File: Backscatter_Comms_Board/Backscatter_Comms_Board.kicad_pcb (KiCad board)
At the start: 2 copper layers, 43 parts, among them J1 Conn_01x03, J2 Conn_01x07, J3 Conn_01x02, M1 MNMOS, M2 MNMOS, T1 SP-48, U1 ADG919BRMZ, U2 ADG841YKSZ-REEL7, U3 NCS2200SQ2T2G

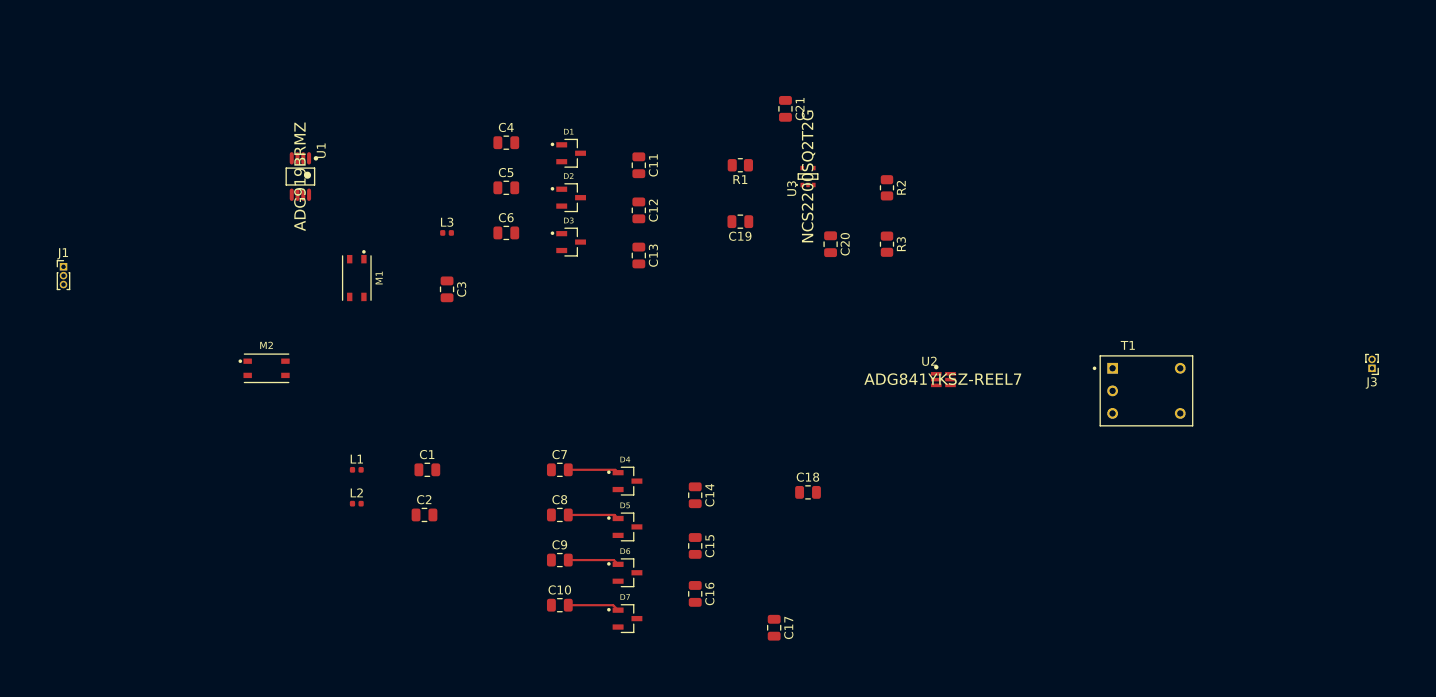
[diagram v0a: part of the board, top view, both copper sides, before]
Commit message: rolled back cause the PCB broke
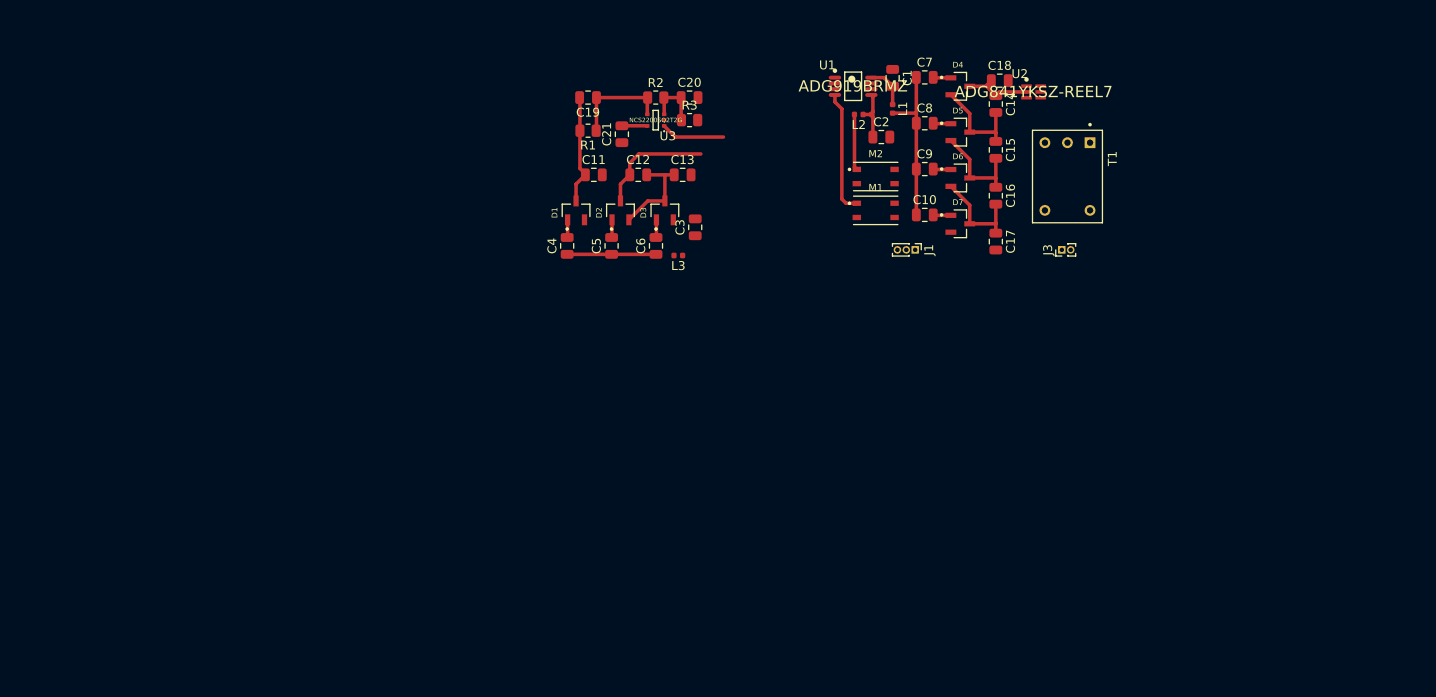
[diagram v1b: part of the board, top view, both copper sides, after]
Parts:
- moved J1 95.9 mm to (137.8, 89.5), turned to 270 degrees
- moved L1 72.7 mm to (135.3, 73.7), turned to 270 degrees
- moved M2 71.9 mm to (133.3, 81.3)
- moved L2 71.5 mm to (131.4, 74.3), turned to 180 degrees
- moved C1 68.5 mm to (135.3, 70.2), turned to 270 degrees
- moved C2 66.8 mm to (134.0, 76.8)
- moved U1 63.1 mm to (130.8, 71.1), turned to 0 degrees
- moved C7 60.3 mm to (138.9, 70.1)
- moved C8 60.3 mm to (138.9, 75.3)
- moved C9 60.2 mm to (138.9, 80.4)
- moved C10 60.2 mm to (138.9, 85.6)
- moved M1 58.9 mm to (133.3, 85.1), turned to 0 degrees
- moved D7 58.1 mm to (142.9, 86.6)
- moved D5 58.1 mm to (142.9, 76.3)
- moved D6 58.1 mm to (142.9, 81.4)
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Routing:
- net Net-(C10-Pad1): track 0.00 -> 18.2 mm
- net Ant: track 0.00 -> 13.9 mm
- net Vrect: track 0.00 -> 13.1 mm
- net Net-(C11-Pad1): track 0.00 -> 12.3 mm
- net Net-(C19-Pad1): track 0.00 -> 11.4 mm
- net Net-(C14-Pad2): track 0.00 -> 11.3 mm
- net Net-(C16-Pad2): track 0.00 -> 11.3 mm
- net Net-(C15-Pad2): track 0.00 -> 11.3 mm
- net Net-(C12-Pad2): track 0.00 -> 11.0 mm
- net Net-(C4-Pad1): track 0.00 -> 10.0 mm
- net Stage4: track 0.00 -> 7.86 mm
- net RF_RX: track 0.00 -> 7.19 mm
- net Net-(C2-Pad1): track 0.00 -> 6.50 mm
- net Net-(C20-Pad1): track 0.00 -> 6.41 mm
- net Net-(J1-Pad3): track 0.00 -> 6.29 mm
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
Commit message: Too big version
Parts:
- added AE1: Antenna_Chip, Connector_Coaxial:U.FL_Molex_MCRF_73412-0110_Vertical, F.Cu at (88.9, 38.1)
- added C22: 0.01uF, Capacitor_SMD:C_0805_2012Metric, F.Cu at (80.6, 35.2)
- J1: value Conn_01x03 -> SPK_IN; footprint Connector_PinHeader_1.00mm:PinHeader_1x03_P1.00mm_Vertical -> Local Components:Multi-purpose_mic
- J2: value Conn_01x07 -> Conn_01x09; footprint Connector_PinHeader_1.00mm:PinHeader_1x07_P1.00mm_Vertical -> Connector_PinHeader_1.00mm:PinHeader_1x09_P1.00mm_Vertical
- M2: value MNMOS -> DNP
- moved T1 88.5 mm to (83.8, 28.6)
- moved J3 87.0 mm to (83.2, 39.4)
- moved J2 81.1 mm to (104.8, 40.6), turned to 90 degrees
- moved M1 69.2 mm to (90.8, 30.5), turned to 90 degrees
- moved J1 67.2 mm to (94.6, 38.1), turned to 0 degrees
- moved C17 64.3 mm to (110.5, 35.6), turned to 0 degrees
- moved C10 62.8 mm to (99.5, 36.7)
- moved C14 62.8 mm to (107.5, 24.2)
- moved C16 62.8 mm to (107.5, 34.5)
- moved C2 62.8 mm to (94.6, 27.9)
- moved C7 62.8 mm to (99.5, 21.2)
- moved C8 62.8 mm to (99.5, 26.4)
- moved C9 62.8 mm to (99.5, 31.5)
- moved D4 62.8 mm to (103.5, 22.2)
- moved D5 62.8 mm to (103.5, 27.4)
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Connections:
- C21 pad 2: Net-(C21-Pad2) -> RX_EN
- J2 pad 1: Stage4 -> Vstore
- J2 pad 2: Vrect -> RX_EN
- J2 pad 3: RF_RX -> Stage4
- J2 pad 4: UPLINK_SR -> Vrect
- J2 pad 5: SPK_EN -> RF_RX
- J2 pad 6: AN_EN -> RF_TX
- J2 pad 7: Ant -> UPLINK_SR
- U3 pad 5: Net-(C21-Pad2) -> RX_EN
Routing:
- net Ant: track 13.9 -> 1.89 mm
- net Net-(J1-Pad3): track 6.29 -> 0.00 mm
- net Net-(C16-Pad2): track 11.3 -> 5.09 mm
- net Vrect: track 13.1 -> 9.76 mm
- net Net-(C11-Pad1): track 12.3 -> 8.97 mm
- net Net-(C12-Pad2): track 11.0 -> 8.03 mm
- net RX_EN: track 0.00 -> 2.87 mm
- net Net-(C21-Pad2): track 2.87 -> 0.00 mm
- net Net-(C10-Pad1): track 18.2 -> 15.5 mm
- net Net-(C14-Pad2): track 11.3 -> 13.3 mm
- net Net-(C15-Pad2): track 11.3 -> 12.1 mm
- added copper zone on B.Cu, net (none)
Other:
- board outline added: 51.4 x 23.5 mm
- board text added: "CHANGE ANT TO UFL CONNECTOR"

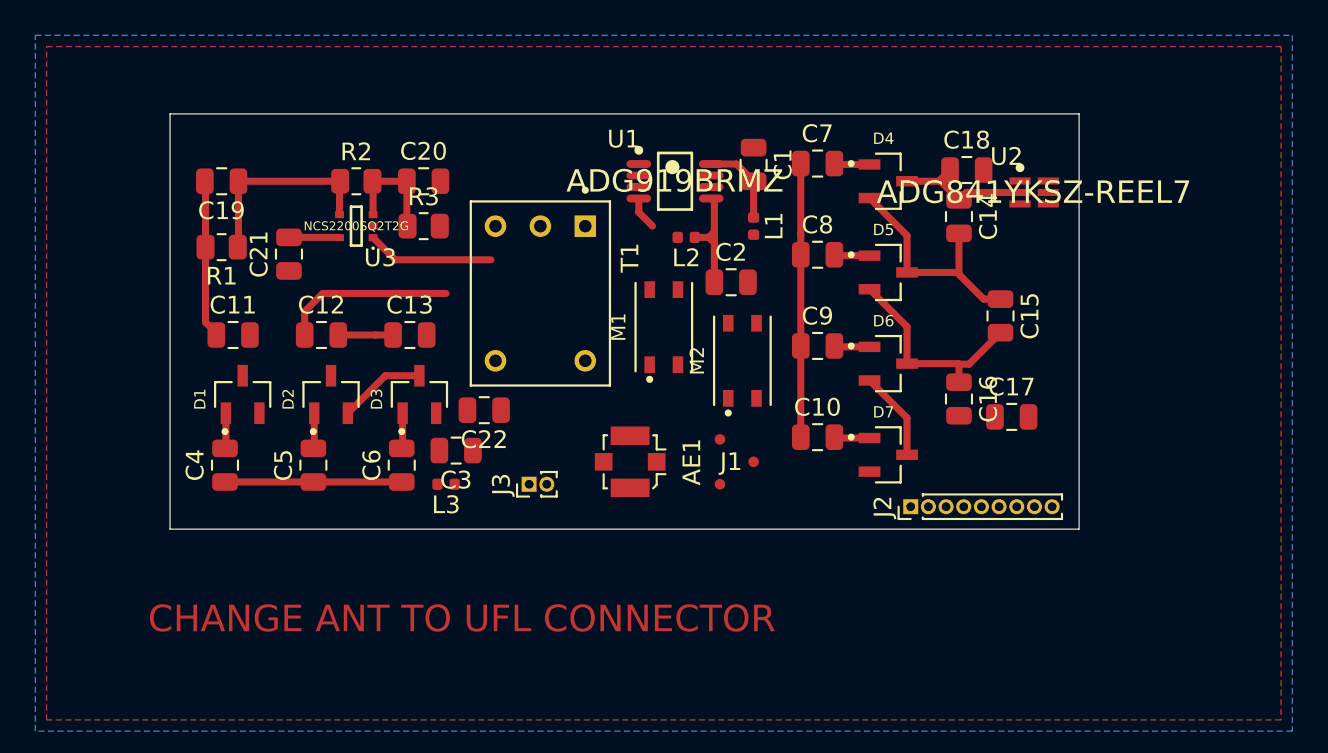
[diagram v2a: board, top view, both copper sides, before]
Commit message: V2 incorporating first round review
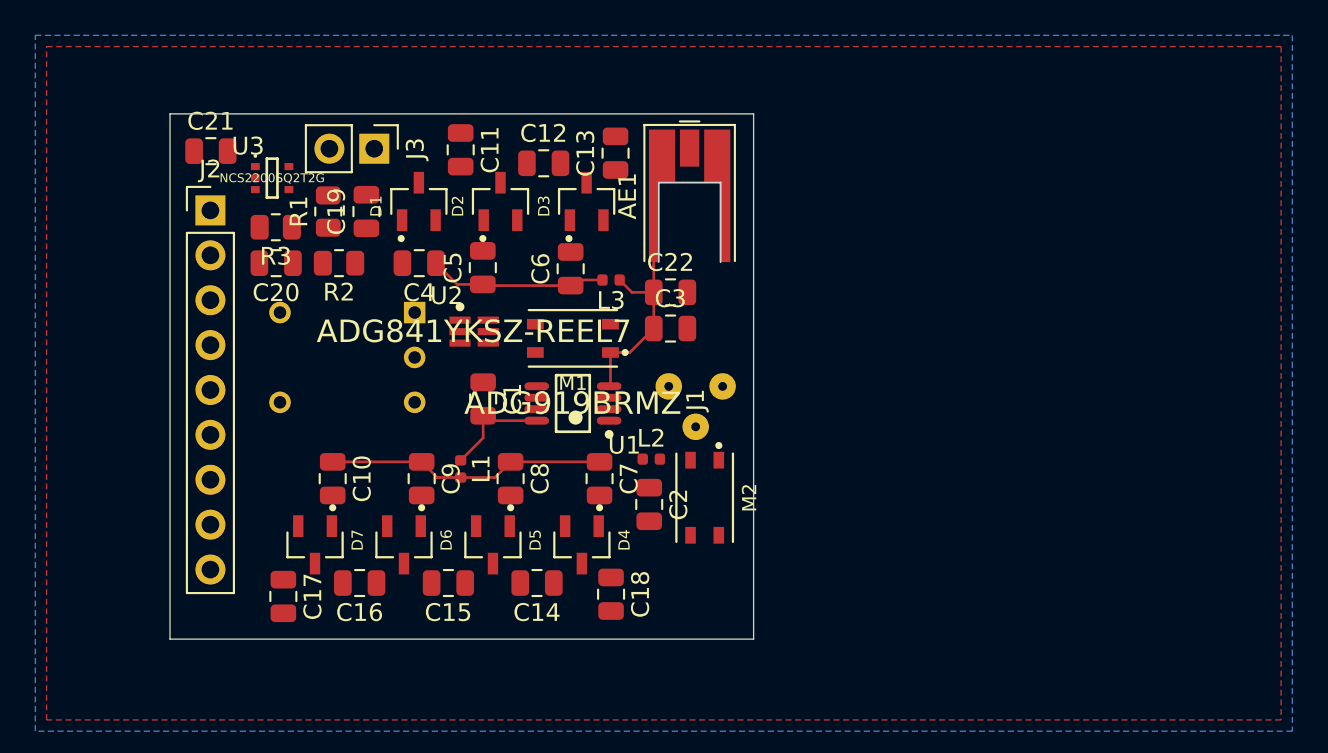
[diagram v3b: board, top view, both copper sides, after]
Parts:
- AE1: footprint Connector_Coaxial:U.FL_Molex_MCRF_73412-0110_Vertical -> Connector_Coaxial:MMCX_Molex_73415-0961_Horizontal_1.0mm-PCB
- J2: footprint Connector_PinHeader_1.00mm:PinHeader_1x09_P1.00mm_Vertical -> Connector_PinHeader_2.54mm:PinHeader_1x09_P2.54mm_Vertical
- J3: footprint Connector_PinHeader_1.00mm:PinHeader_1x02_P1.00mm_Vertical -> Connector_PinHeader_2.54mm:PinHeader_1x02_P2.54mm_Vertical
- T1: moved to B.Cu
- moved J2 43.0 mm to (65.2, 23.9), turned to 0 degrees
- moved C17 42.4 mm to (69.3, 45.7), turned to 270 degrees
- moved C16 35.5 mm to (73.6, 45.0), turned to 180 degrees
- moved C15 34.7 mm to (78.6, 45.0), turned to 180 degrees
- moved D7 32.8 mm to (71.1, 42.8), turned to 270 degrees
- moved U2 32.7 mm to (80.1, 30.7)
- moved C14 31.6 mm to (83.6, 45.0), turned to 180 degrees
- moved C18 31.3 mm to (87.8, 45.6), turned to 270 degrees
- moved D6 29.3 mm to (76.1, 42.8), turned to 270 degrees
- moved C10 27.5 mm to (72.1, 39.1), turned to 270 degrees
- moved D5 27.2 mm to (81.1, 42.8), turned to 270 degrees
- moved D4 26.9 mm to (86.2, 42.8), turned to 270 degrees
- moved C9 23.6 mm to (77.1, 39.1), turned to 270 degrees
- moved C7 21.7 mm to (87.2, 39.1), turned to 270 degrees
- moved L1 21.5 mm to (79.3, 38.5)
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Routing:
- net Ant: track 1.89 -> 17.1 mm
- net Net-(C14-Pad2): track 13.3 -> 0.00 mm
- net Net-(C15-Pad2): track 12.1 -> 0.00 mm
- net Net-(C19-Pad1): track 11.4 -> 0.00 mm
- net Vrect: track 9.76 -> 0.00 mm
- net Net-(C11-Pad1): track 8.97 -> 0.00 mm
- net Net-(C12-Pad2): track 8.03 -> 0.00 mm
- net Stage4: track 7.86 -> 0.00 mm
- net RF_RX: track 7.19 -> 0.00 mm
- net Net-(C2-Pad1): track 6.50 -> 0.00 mm
- net Net-(C20-Pad1): track 6.41 -> 0.00 mm
- net Net-(C16-Pad2): track 5.09 -> 0.00 mm
- net RX_EN: track 2.87 -> 0.00 mm
- net Net-(C6-Pad2): track 2.01 -> 0.00 mm
- net Net-(C5-Pad2): track 2.01 -> 0.00 mm
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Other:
- board size 51.4 x 23.5 mm -> 33 x 29.7 mm
- net class Default: clearance 0.2 -> 0.1524; trace_width 0.25 -> 0.1524
- rule trace_clearance: 0.2 -> 0.1524
- rule trace_min: 0.2 -> 0.1524
- board text removed: "CHANGE ANT TO UFL CONNECTOR"

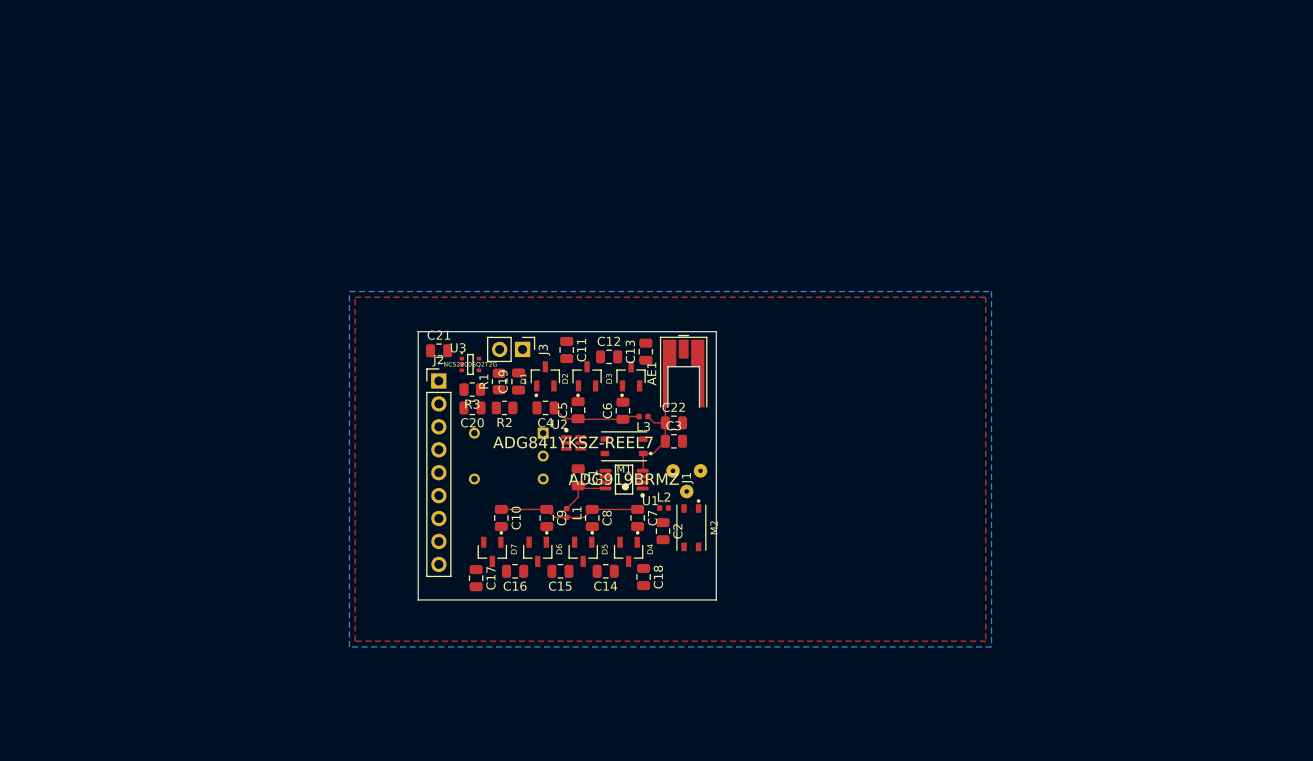
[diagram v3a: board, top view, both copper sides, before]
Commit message: Redid Board layou
Even smaller rf path and other fun things
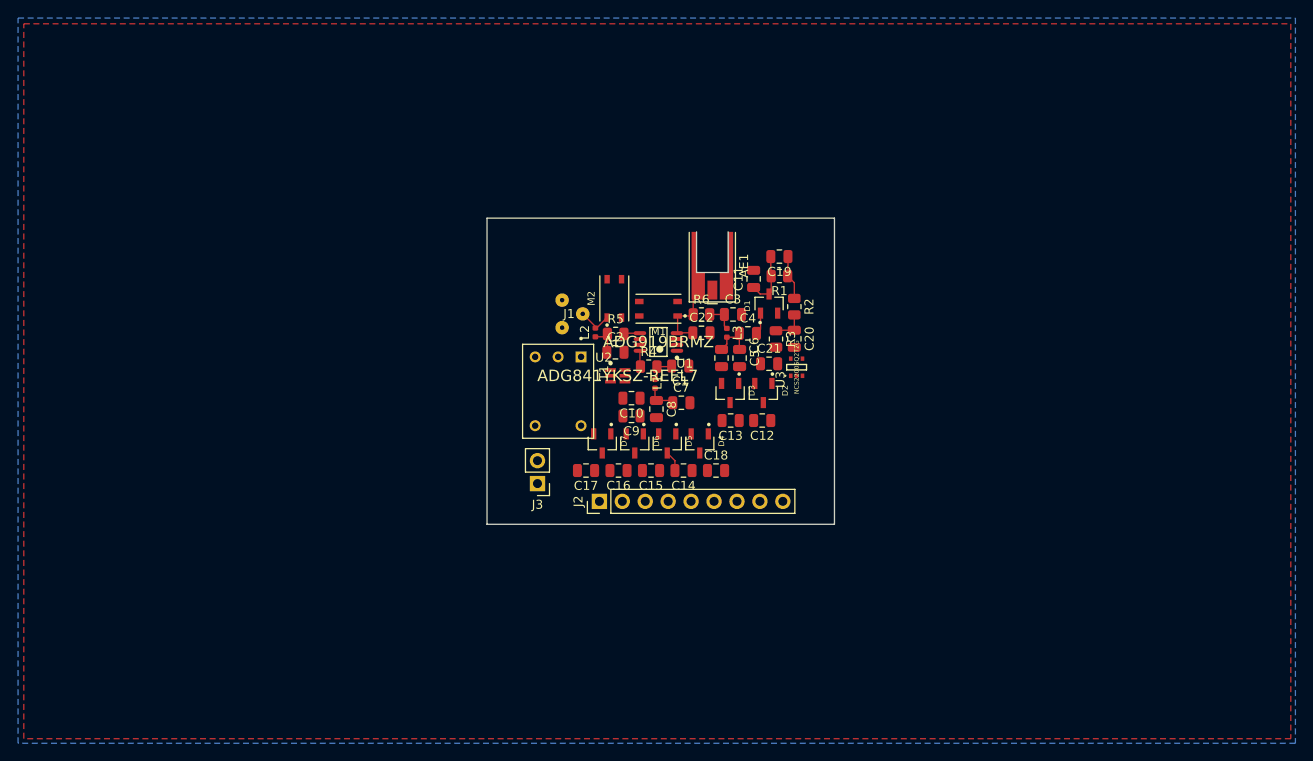
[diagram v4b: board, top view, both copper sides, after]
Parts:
- added R4: 0, Resistor_SMD:R_0805_2012Metric, F.Cu at (88.4, 22.3)
- added R5: 0, Resistor_SMD:R_0805_2012Metric, F.Cu at (84.7, 18.7)
- added R6: 0, Resistor_SMD:R_0805_2012Metric, F.Cu at (94.2, 16.5)
- T1: moved to F.Cu
- moved C21 36.6 mm to (101.7, 22.0)
- moved C20 36.5 mm to (104.5, 19.2), turned to 270 degrees
- moved U3 36.1 mm to (104.8, 22.4), turned to 90 degrees
- moved R3 34.1 mm to (102.5, 19.2), turned to 270 degrees
- moved R2 34.0 mm to (104.5, 15.6), turned to 270 degrees
- moved R1 33.2 mm to (102.9, 12.3), turned to 180 degrees
- moved C19 32.0 mm to (102.9, 10.1), turned to 180 degrees
- moved M2 26.8 mm to (84.6, 14.7), turned to 90 degrees
- moved D1 26.1 mm to (101.7, 15.3)
- moved C4 23.9 mm to (99.4, 18.6), turned to 0 degrees
- moved J1 22.3 mm to (79.6, 16.4), turned to 0 degrees
- moved J2 22.2 mm to (82.9, 37.2), turned to 90 degrees
- moved C11 22.1 mm to (100.0, 12.6), turned to 90 degrees
- moved L2 20.9 mm to (82.5, 18.5), turned to 90 degrees
- moved C2 20.5 mm to (84.7, 20.7), turned to 0 degrees
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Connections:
- C3 pad 1: Ant -> Net-(C3-Pad1)
- L3 pad 1: Ant -> Net-(C3-Pad1)
- U1 pad 5: Net-(C2-Pad1) -> Net-(R5-Pad1)
- U1 pad 8: Net-(C1-Pad2) -> Net-(R4-Pad1)
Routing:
- net Net-(C10-Pad1): track 15.8 -> 3.52 mm
- net Ant: track 17.1 -> 8.89 mm
- net Net-(C11-Pad1): track 0.00 -> 6.27 mm
- net Net-(C4-Pad1): track 10.1 -> 4.95 mm
- net Net-(C19-Pad1): track 0.00 -> 4.96 mm
- net Net-(C20-Pad1): track 0.00 -> 4.23 mm
- net Net-(J1-Pad3): track 0.00 -> 3.92 mm
- net Net-(C2-Pad1): track 0.00 -> 3.52 mm
- net Net-(C3-Pad1): track 0.00 -> 3.29 mm
- net Net-(C1-Pad2): track 6.20 -> 3.16 mm
- net Net-(C4-Pad2): track 0.00 -> 2.43 mm
- net Net-(C14-Pad2): track 0.00 -> 2.29 mm
- net Net-(R5-Pad1): track 0.00 -> 1.81 mm
- net Net-(R4-Pad1): track 0.00 -> 1.78 mm
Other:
- board size 33 x 29.7 mm -> 38.5 x 33.9 mm
